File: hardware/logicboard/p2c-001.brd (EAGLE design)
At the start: 91 x 55 mm, 50 parts, among them IC1 74LS07N, K1 G5V1, T1 2SC1815

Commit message: Added "How to use."
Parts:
- added U$5: HELP_P2C, pineapple:HELP_P2C
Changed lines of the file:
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@@
 <grid distance="1" unitdist="mm" unit="mm" style="lines" multiple="1" display="yes" altdistance="5" altunitdist="mil" altunit="mil"/>
 <layers>
-<layer number="1" name="Top" color="4" fill="1" visible="yes" active="yes"/>
-<layer number="16" name="Bottom" color="1" fill="1" visible="yes" active="yes"/>
+<layer number="1" name="Top" color="4" fill="1" visible="no" active="yes"/>
+<layer number="16" name="Bottom" color="1" fill="1" visible="no" active="yes"/>
 <layer number="17" name="Pads" color="2" fill="1" visible="yes" active="yes"/>
 <layer number="18" name="Vias" color="2" fill="1" visible="yes" active="yes"/>
 <layer number="19" name="Unrouted" color="6" fill="1" visible="yes" active="yes"/>
 <layer number="20" name="Dimension" color="24" fill="1" visible="yes" active="yes"/>
-<layer number="21" name="tPlace" color="7" fill="1" visible="yes" active="yes"/>
+<layer number="21" name="tPlace" color="7" fill="1" visible="no" active="yes"/>
 <layer number="22" name="bPlace" color="7" fill="1" visible="yes" active="yes"/>
 <layer number="23" name="tOrigins" color="15" fill="1" visible="yes" active="yes"/>
@@
 <attribute name="VALUE" x="3.27" y="9.27" size="0.6096" layer="28" font="vector" ratio="20" rot="MR270"/>
 </element>
+<element name="U$5" library="pineapple" package="HELP_P2C" value="HELP_P2C" x="48" y="36" rot="MR0"/>
 </elements>
 <signals>

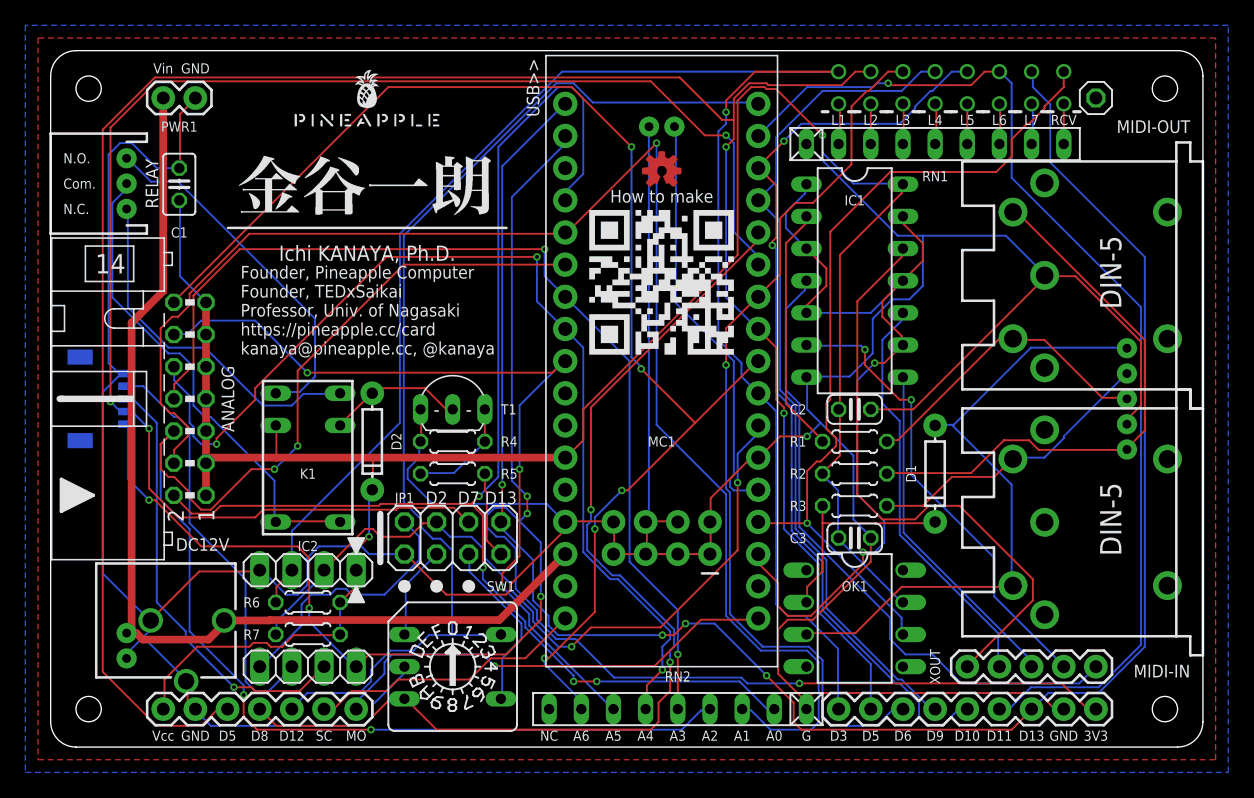
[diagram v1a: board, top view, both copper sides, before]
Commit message: Fixed QR code.
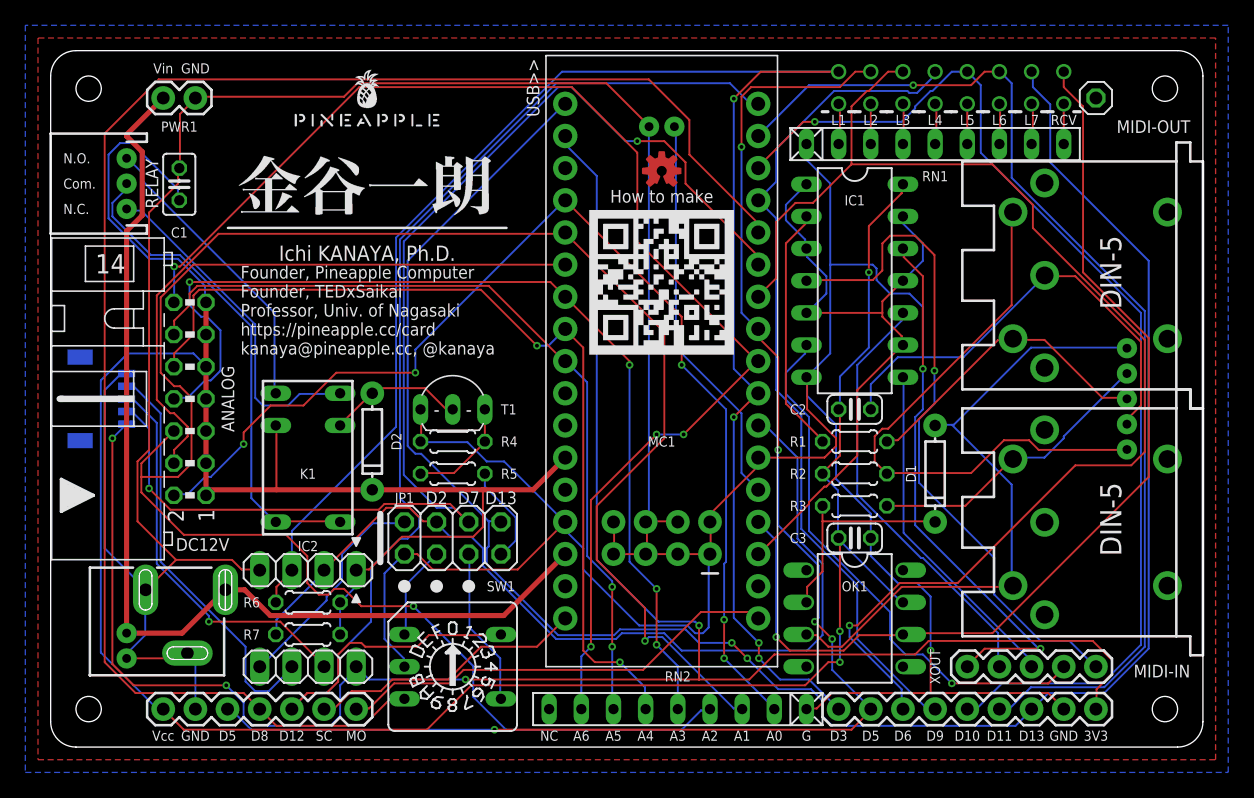
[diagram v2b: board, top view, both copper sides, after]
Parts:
- DC12V: value POWER_JACKPTH_BREAD -> POWER_JACKSLT; device SparkFun-Connectors:POWER_JACK_PTH_BREAD -> SparkFun-Connectors:POWER_JACK_SLOT
- moved DC12V 5.00 mm to (0.00, 15.0)
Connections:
- net GND: now also DC12V.GND@1, DC12V.GND@2; no longer DC12V.GND, DC12V.GNDBREAK
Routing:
- net VCC: track 179.2 -> 237.8 mm, vias 2 -> 3
- net PWM_1: track 173.0 -> 116.1 mm, vias 2 -> 5
- net SW_2: track 82.2 -> 128.8 mm, vias 2 -> 0
- net GND: track 344.6 -> 376.6 mm
- net PWM_2: track 70.8 -> 100.3 mm
- net SW_1: track 120.5 -> 99.2 mm, vias 3 -> 2
- net ANLG_1: track 118.2 -> 98.6 mm
- net MIDIOUT: track 69.2 -> 53.1 mm, vias 2 -> 0
- net ANLG_0: track 105.3 -> 89.3 mm, vias 4 -> 5
- net MIDIIN: track 65.7 -> 80.0 mm
- net SW_0: track 60.4 -> 73.6 mm, vias 2 -> 0
- net PWM_4: track 73.7 -> 86.8 mm, vias 2 -> 1
- net SW_3: track 86.6 -> 97.7 mm
- net VDD: track 149.7 -> 160.3 mm, vias 6 -> 4
- net ANLG_4: track 81.7 -> 72.0 mm, vias 3 -> 2
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
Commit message: Slightly moved external pins.
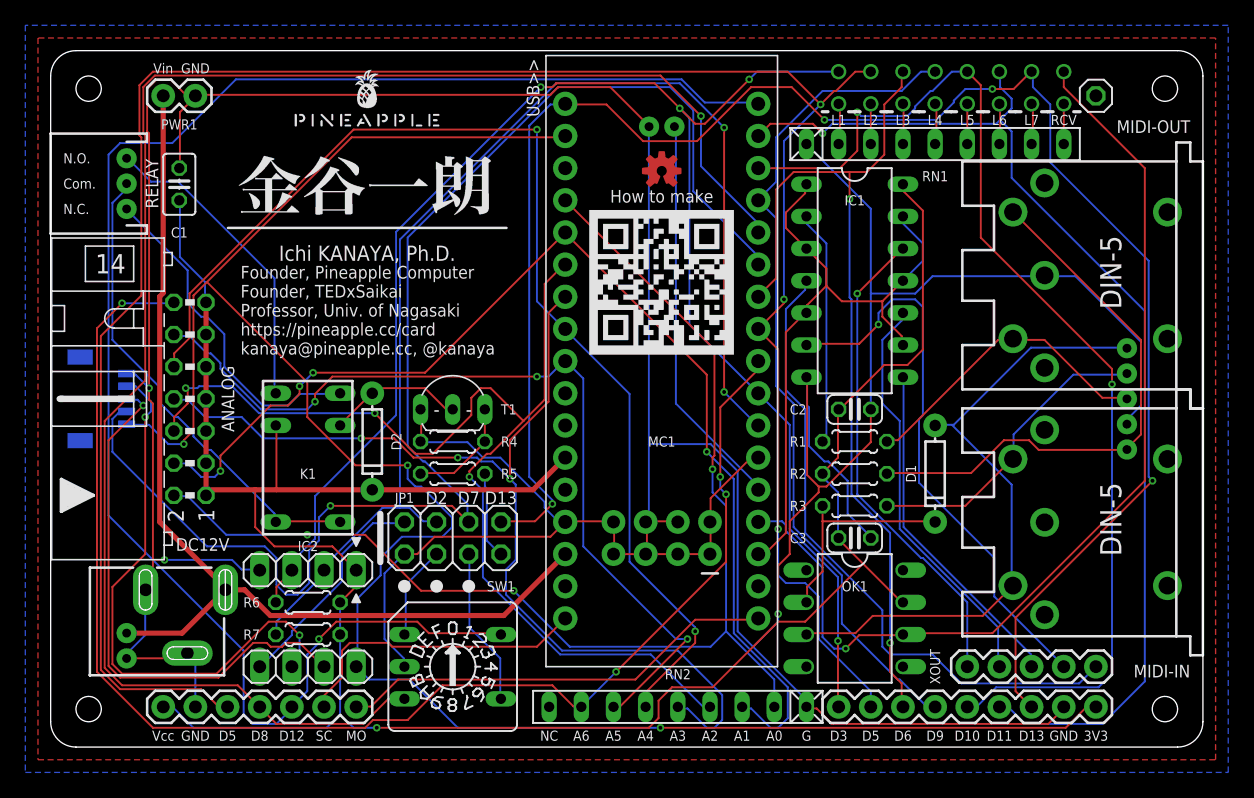
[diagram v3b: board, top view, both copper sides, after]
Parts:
- moved POGOPIN 0.18 mm to (82.5, 51.4)
- moved PWR1 0.18 mm to (8.89, 51.4)
- moved DIGITAL 0.17 mm to (82.5, 3.17)
- moved LIGHTDRIVE 0.17 mm to (8.89, 3.17)
- moved RN2 0.17 mm to (49.5, 3.17)
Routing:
- net PWM_1: track 116.1 -> 173.3 mm, vias 5 -> 3
- net VCC: track 237.8 -> 187.7 mm, vias 3 -> 1
- net SW_3: track 97.7 -> 129.6 mm, vias 0 -> 1
- net PWM_2: track 100.3 -> 70.0 mm, vias 1 -> 2
- net ANLG_2: track 114.1 -> 87.5 mm, vias 1 -> 3
- net SW_0: track 73.6 -> 96.3 mm, vias 0 -> 2
- net ANLG_4: track 72.0 -> 91.5 mm
- net PWM_6: track 156.1 -> 140.6 mm, vias 2 -> 4
- net SW_1: track 99.2 -> 111.2 mm, vias 2 -> 1
- net SDA: track 32.4 -> 44.4 mm, vias 0 -> 2
- net SCL: track 31.2 -> 42.8 mm
- net GND: track 376.6 -> 367.9 mm, vias 1 -> 3
- net PWM_0: track 136.9 -> 128.5 mm
- net ANLG_1: track 98.6 -> 90.7 mm, vias 1 -> 4
- net ANLG_6: track 102.5 -> 109.8 mm
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
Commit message: Changed routing.
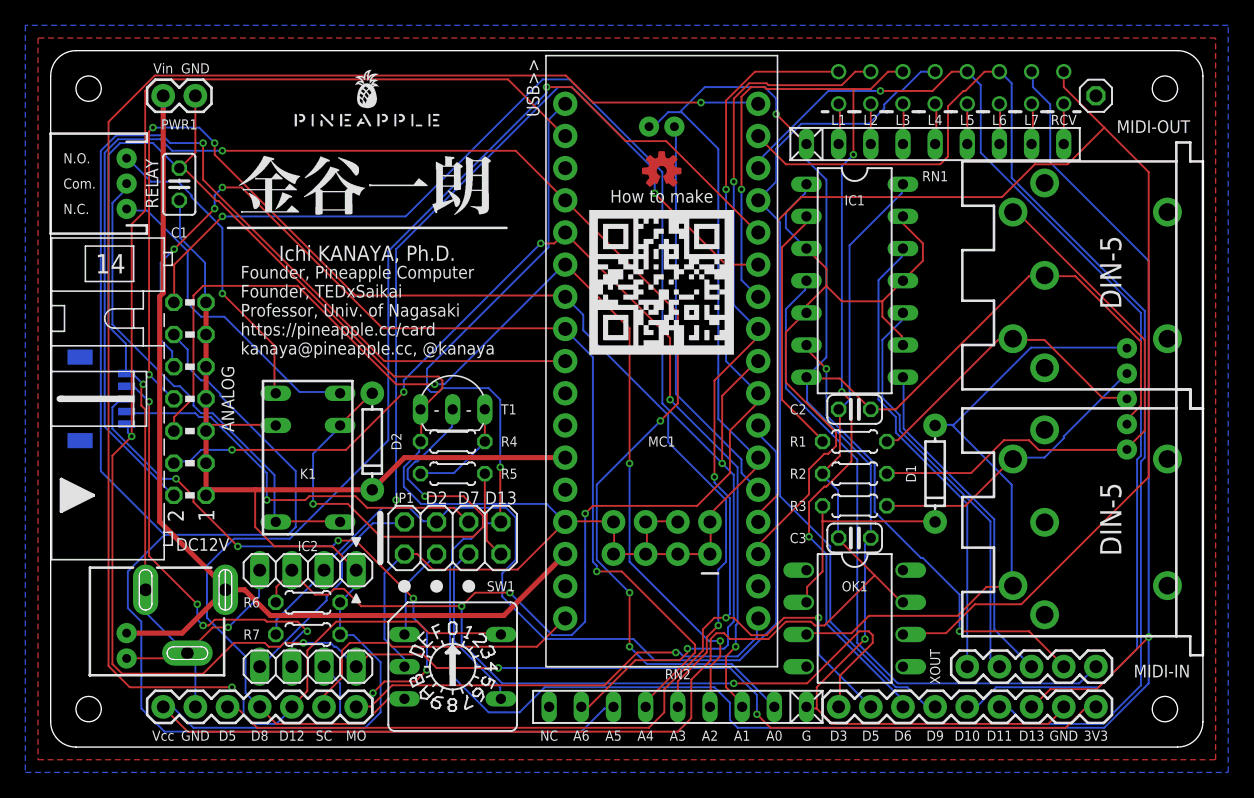
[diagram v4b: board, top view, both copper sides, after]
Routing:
- net ANLG_5: track 70.2 -> 163.0 mm, vias 3 -> 1
- net PWM_1: track 173.3 -> 118.6 mm, vias 3 -> 4
- net PWM_6: track 140.6 -> 182.3 mm, vias 4 -> 2
- net MIDIIN: track 78.7 -> 112.6 mm, vias 1 -> 0
- net SW_2: track 130.4 -> 98.7 mm
- net RELAYTR: track 10.8 -> 40.6 mm, vias 0 -> 2
- net GND: track 367.9 -> 338.2 mm, vias 3 -> 4
- net ANLG_0: track 96.1 -> 124.2 mm, vias 3 -> 4
- net SW_0: track 96.3 -> 73.2 mm, vias 2 -> 0
- net VCC: track 187.7 -> 208.7 mm, vias 1 -> 0
- net ANLG_3: track 81.9 -> 100.2 mm, vias 3 -> 4
- net SW_1: track 111.2 -> 93.3 mm, vias 1 -> 3
- net PWM_2: track 70.0 -> 84.1 mm, vias 2 -> 4
- net SCL: track 42.8 -> 53.3 mm, vias 1 -> 6
- net SDA: track 44.4 -> 34.0 mm, vias 2 -> 4
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
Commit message: Moved pinheaders slightly.
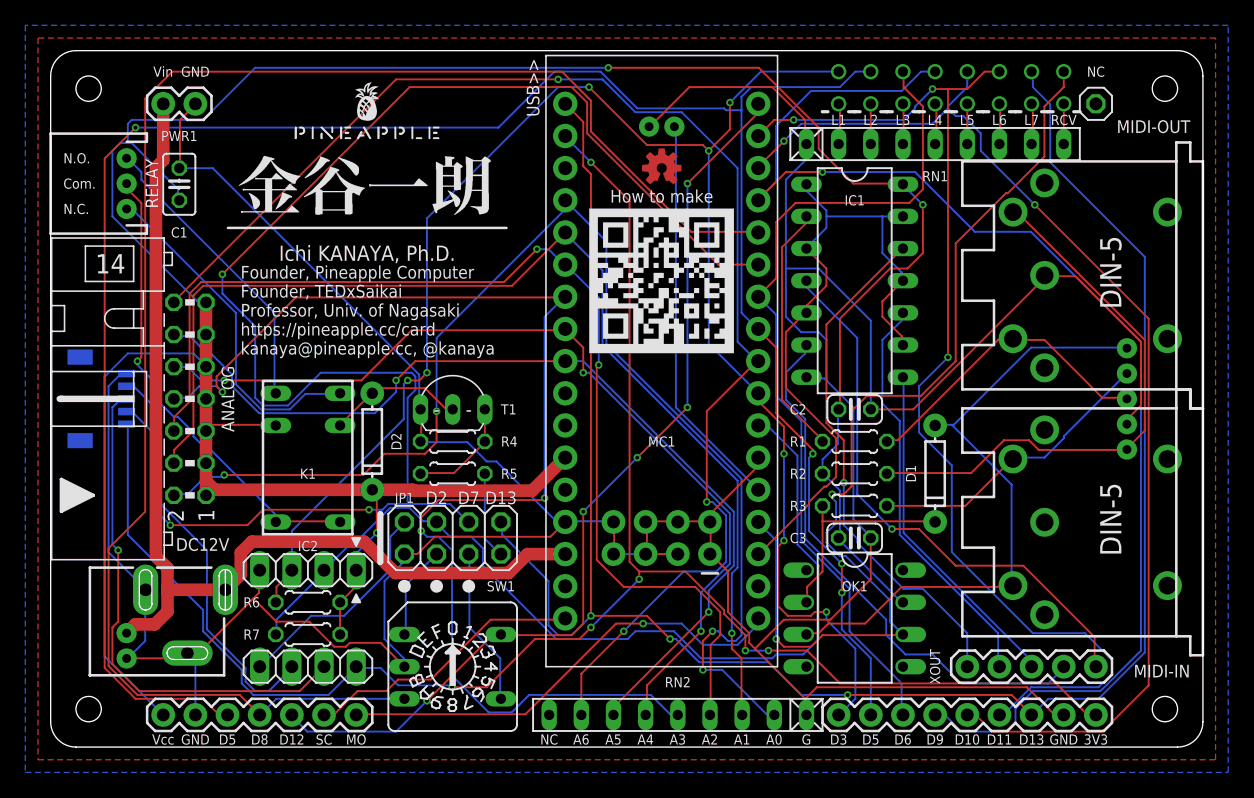
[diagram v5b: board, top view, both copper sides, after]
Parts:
- removed POGOPIN: (no value), pinhead:1X01
- added NC: (no value), pinhead:1X01
- moved U$1 1.00 mm to (25.0, 48.0)
- moved PWR1 0.64 mm to (8.89, 50.8)
- moved DIGITAL 0.63 mm to (82.5, 2.54)
- moved LIGHTDRIVE 0.63 mm to (8.89, 2.54)
- moved RN2 0.63 mm to (49.5, 2.54)
- moved LOGO1 0.22 mm to (48.3, 45.7)
- moved U$4 0.11 mm to (48.3, 36.8)
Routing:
- net ANLG_5: track 163.0 -> 74.5 mm, vias 1 -> 2
- net SW_3: track 136.1 -> 74.0 mm, vias 2 -> 5
- net PWM_1: track 118.6 -> 170.2 mm
- net PWM_3: track 66.6 -> 102.0 mm, vias 0 -> 1
- net MIDIIN: track 112.6 -> 78.8 mm, vias 0 -> 2
- net SW_1: track 93.3 -> 126.4 mm
- net RELAYTR: track 40.6 -> 10.8 mm, vias 2 -> 0
- net SW_2: track 98.7 -> 127.5 mm, vias 1 -> 0
- net PWM_6: track 182.3 -> 154.0 mm, vias 2 -> 3
- net VDD: track 167.3 -> 140.2 mm, vias 4 -> 6
- net VCC: track 208.7 -> 235.7 mm, vias 0 -> 3
- net ANLG_0: track 124.2 -> 99.5 mm
- net GND: track 338.2 -> 319.3 mm, vias 4 -> 0
- net PWM_2: track 84.1 -> 66.9 mm, vias 4 -> 0
- net ANLG_4: track 85.2 -> 71.9 mm, vias 4 -> 3
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
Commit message: Changed pattern.
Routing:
- net SCL: track 40.5 -> 141.2 mm, vias 1 -> 15
- net VCC: track 235.7 -> 167.2 mm, vias 3 -> 4
- net SW_3: track 74.0 -> 131.5 mm, vias 5 -> 0
- net ANLG_4: track 71.9 -> 111.6 mm, vias 3 -> 2
- net PWM_3: track 102.0 -> 66.8 mm, vias 1 -> 0
- net PWM_2: track 66.9 -> 101.6 mm, vias 0 -> 1
- net ANLG_1: track 89.6 -> 115.0 mm, vias 1 -> 4
- net GND: track 319.3 -> 343.4 mm, vias 0 -> 1
- net PWM_6: track 154.0 -> 137.9 mm, vias 3 -> 6
- net ANLG_6: track 107.6 -> 92.5 mm, vias 3 -> 4
- net SW_1: track 126.4 -> 112.7 mm, vias 3 -> 5
- net ANLG_2: track 87.4 -> 78.5 mm, vias 2 -> 6
- net SW_0: track 74.0 -> 65.9 mm, vias 0 -> 2
- net PWM_0: track 131.1 -> 139.1 mm, vias 8 -> 5
- net SDA: track 32.4 -> 39.9 mm
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
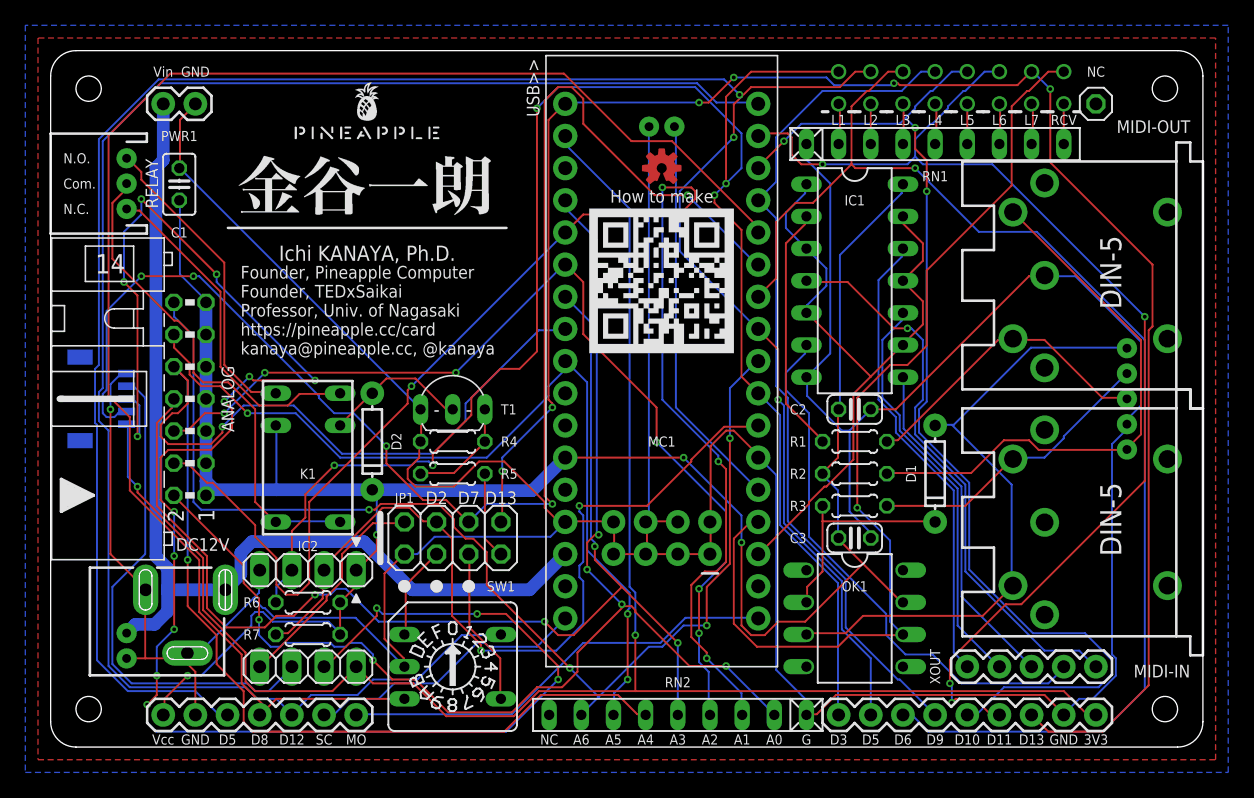
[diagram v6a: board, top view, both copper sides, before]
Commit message: Now power lines are also autorouted.
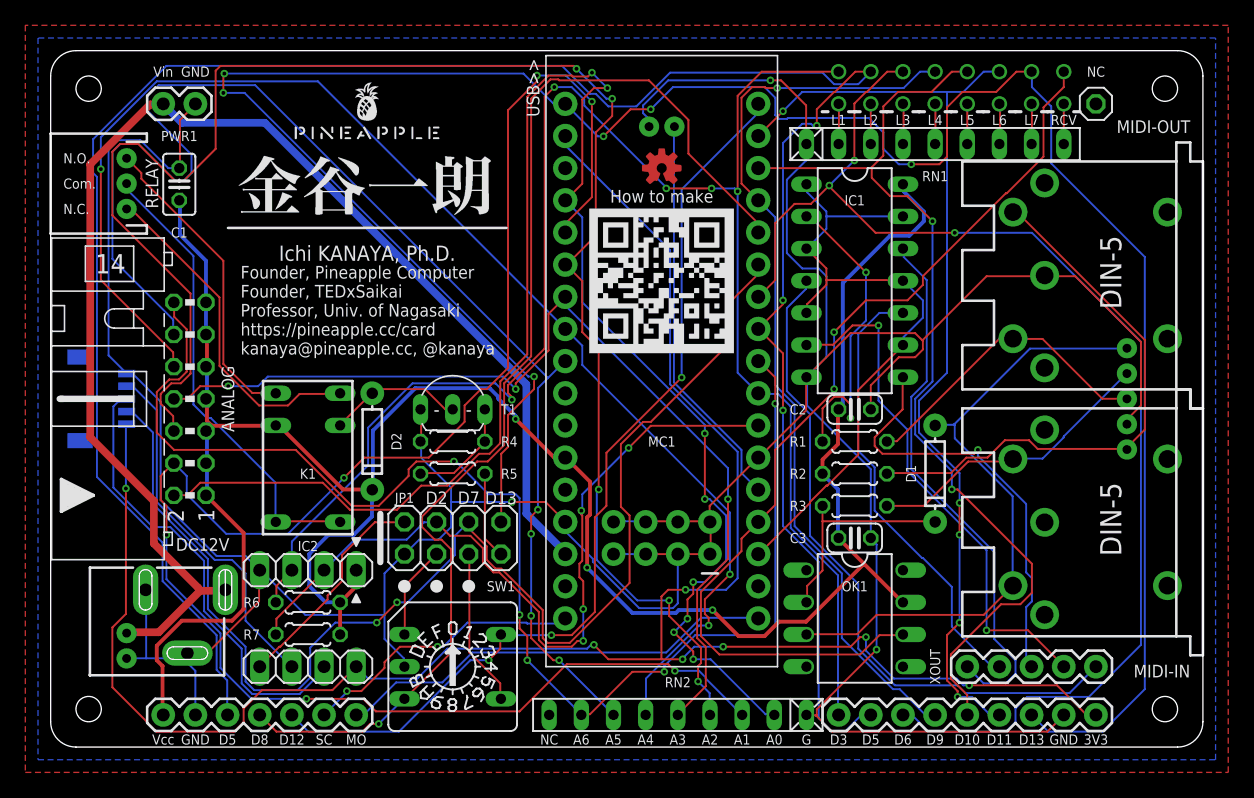
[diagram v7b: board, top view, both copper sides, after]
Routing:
- net SCL: track 141.2 -> 36.0 mm, vias 15 -> 0
- net SW_3: track 131.5 -> 74.6 mm, vias 0 -> 3
- net ANLG_2: track 78.5 -> 132.7 mm, vias 6 -> 5
- net PWM_6: track 137.9 -> 188.2 mm
- net ANLG_5: track 71.0 -> 105.5 mm, vias 3 -> 4
- net GND: track 343.4 -> 314.1 mm, vias 1 -> 3
- net SW_2: track 121.9 -> 92.9 mm, vias 0 -> 1
- net ANLG_0: track 100.8 -> 128.9 mm, vias 6 -> 8
- net ANLG_1: track 115.0 -> 140.6 mm, vias 4 -> 6
- net VIN: track 81.3 -> 106.8 mm
- net VDD: track 141.9 -> 161.2 mm, vias 2 -> 7
- net VCC: track 167.2 -> 184.3 mm, vias 4 -> 3
- net ANLG_3: track 93.2 -> 77.6 mm, vias 4 -> 3
- net PWM_5: track 90.3 -> 75.8 mm, vias 4 -> 5
- net ANLG_6: track 92.5 -> 105.2 mm, vias 4 -> 5
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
